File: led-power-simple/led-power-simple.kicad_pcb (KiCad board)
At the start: 2 copper layers, 84.3 x 84.3 mm, 38 parts, among them J1 Screw_Terminal_01x02, J2 Screw_Terminal_01x02, J3 Screw_Terminal_01x02, J4 Screw_Terminal_01x02, J5 Screw_Terminal_01x02, J6 Screw_Terminal_01x02, J7 Screw_Terminal_01x02, J8 Screw_Terminal_01x02, J9 Screw_Terminal_01x02, U1 LM7809_TO220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

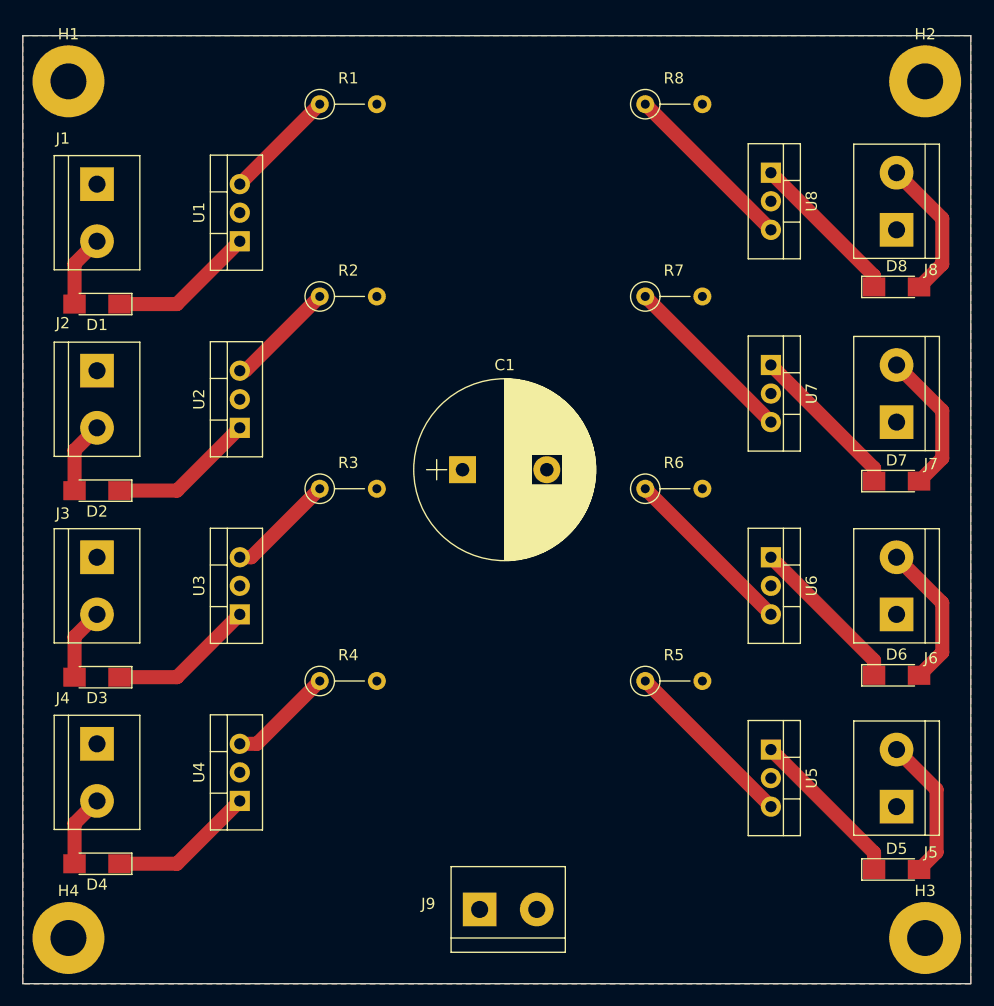
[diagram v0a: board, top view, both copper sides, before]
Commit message: protective mosfet on power input. all THT parts
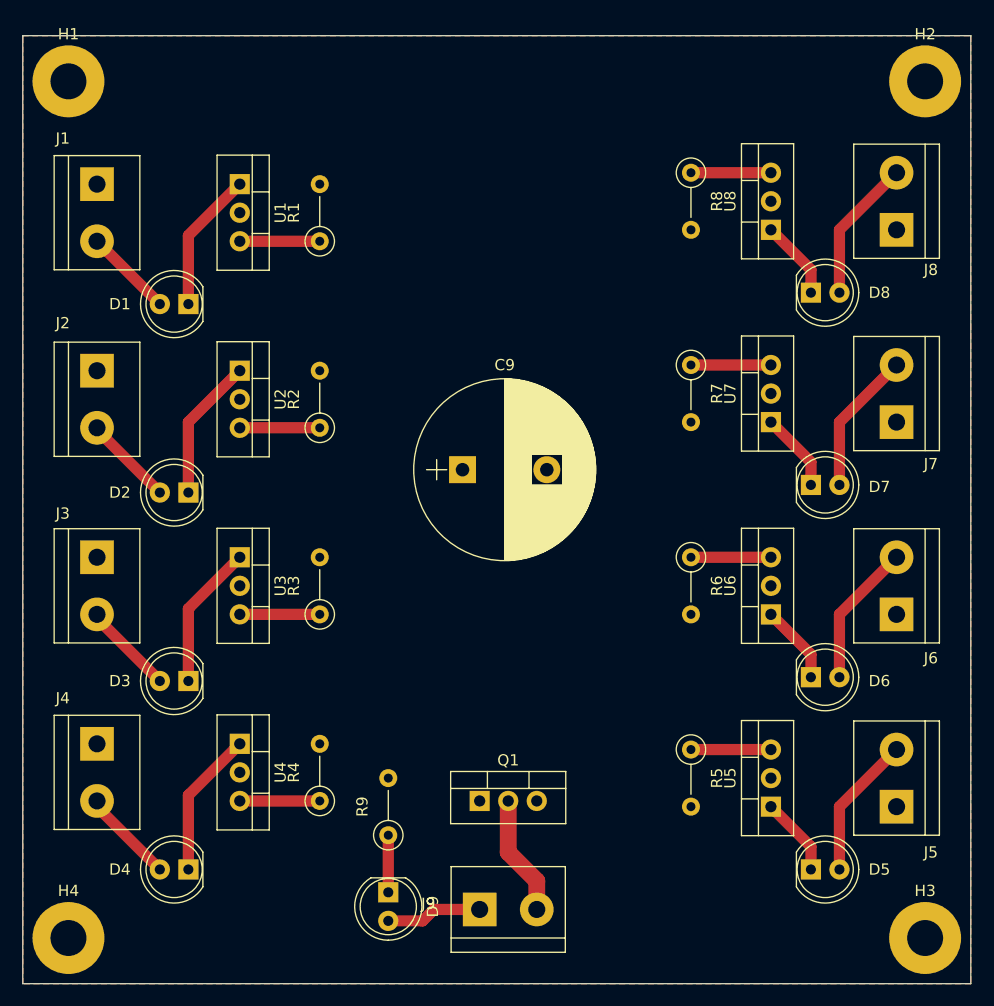
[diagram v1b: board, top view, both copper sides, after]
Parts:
- added D9: LED_Small, LEDs:LED_D5.0mm, F.Cu at (104.6, 148.3)
- added Q1: IRF740, TO_SOT_Packages_THT:TO-220-3_Vertical, F.Cu at (112.8, 140.2)
- added R9: 450, Resistors_THT:R_Axial_DIN0207_L6.3mm_D2.5mm_P5.08mm_Vertical, F.Cu at (104.6, 143.3)
- D1, D2, D3, D4, D5, D6, D7, D8: footprint LEDs:LED_1206_HandSoldering -> LEDs:LED_D5.0mm
- R1, R2, R3, R4, R5, R6, R7, R8: value 250 -> 450
- moved R1 12.2 mm to (98.6, 90.4), turned to 90 degrees
- moved R2 11.7 mm to (98.6, 107.0), turned to 90 degrees
- moved R3 11.2 mm to (98.6, 123.6), turned to 90 degrees
- moved R4 10.7 mm to (98.6, 140.2), turned to 90 degrees
- moved D4 8.14 mm to (86.9, 146.3)
- moved D3 8.14 mm to (86.9, 129.5)
- moved D2 8.13 mm to (86.9, 112.8)
- moved D1 8.13 mm to (86.9, 96.0)
- moved D8 7.64 mm to (142.2, 95.0)
- moved D7 7.63 mm to (142.2, 112.1)
- moved D6 7.62 mm to (142.2, 129.2)
- moved D5 7.62 mm to (142.2, 146.3)
- moved R5 7.33 mm to (131.6, 135.6), turned to 270 degrees
- moved R6 7.33 mm to (131.6, 118.5), turned to 270 degrees
- moved R7 7.33 mm to (131.6, 101.4), turned to 270 degrees
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- renumbered C1 to C9
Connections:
- J9 pad 2: GND -> Net-(J9-Pad2)
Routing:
- net Net-(J9-Pad2): track 0.00 -> 10.7 mm
- net Net-(R5-Pad1): track 15.8 -> 7.11 mm
- net Net-(R8-Pad1): track 15.8 -> 7.11 mm
- net Net-(R7-Pad1): track 15.8 -> 7.11 mm
- net Net-(R6-Pad1): track 15.8 -> 7.11 mm
- net +48V: track 0.00 -> 8.55 mm
- net Net-(D5-Pad1): track 14.5 -> 7.06 mm
- net Net-(D6-Pad1): track 14.3 -> 7.06 mm
- net Net-(D7-Pad1): track 14.1 -> 7.06 mm
- net Net-(D8-Pad1): track 14.0 -> 7.06 mm
- net Net-(D9-Pad1): track 0.00 -> 5.08 mm
- net Net-(R1-Pad1): track 10.1 -> 7.11 mm
- net Net-(R2-Pad1): track 9.85 -> 7.11 mm
- net Net-(R3-Pad1): track 9.64 -> 7.11 mm
- net Net-(R4-Pad1): track 9.43 -> 7.11 mm
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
